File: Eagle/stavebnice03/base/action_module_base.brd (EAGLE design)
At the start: 16 parts

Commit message: I did an order in Eagle files
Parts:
- removed C1, C3, C4, C5: 100nF, resistor:C0603
- removed R1, R2: 4k7, resistor:M0805
- removed U$2, U$3, U$6, U$7: NC7SB3157P6X, !stavebnice03:SC70-6L
- removed U$5: JUMPER5F-90, !stavebnice03:JUMPER5F-90
- added R3: 2K2, resistor:R0603
- added R4: 2k2, resistor:R0603
- moved C2 2.53 mm to (7.50, 9.70), turned to 270 degrees
- moved U$1 0.43 mm to (3.90, 13.3)
- moved U$9 0.25 mm to (5.50, 1.50)
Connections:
- removed net N$1 (its old number): U$1.3, U$6.6, U$7.6
- removed net N$10: R2.1, U$5.2, U$6.3, U$7.1
- removed net N$20: U$2.3, U$7.4
- removed net N$4: U$1.9, U$3.4
- removed net N$6: R1.1, U$5.4, U$6.1, U$7.3
- removed net N$7: U$3.3, U$6.4
- removed net N$8: U$3.1, U$4.2
- removed net N$9: U$1.2, U$2.6, U$3.6
- net GND: no longer C1.2, C3.1, C4.2, C5.1, U$2.2, U$3.2, U$5.1, U$5.5, U$6.2, U$7.2
- net N$2: now also R3.1, U$4.2; no longer U$2.4
- net N$5: now also R4.1, U$1.9; no longer U$2.1
- net VCC: now also R3.2, R4.2, U$1.2, U$1.3; no longer C1.1, C3.2, C4.1, C5.2, R1.2, R2.2, U$2.5, U$3.5, U$5.3, U$6.5, U$7.5
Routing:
- net GND: track 82.6 -> 23.9 mm, vias 2 -> 0
- net N$4: track 27.1 -> 0.00 mm, vias 2 -> 0
- net N$1 (its old number): track 24.3 -> 0.00 mm
- net N$9: track 21.2 -> 0.00 mm, vias 2 -> 0
- net N$20: track 17.6 -> 0.00 mm, vias 2 -> 0
- net N$2: track 9.18 -> 23.1 mm, vias 2 -> 0
- net VCC: track 51.9 -> 39.7 mm, vias 3 -> 0
- net N$13: track 21.8 -> 33.0 mm
- net N$6: track 10.2 -> 0.00 mm, vias 1 -> 0
- net N$10: track 9.64 -> 0.00 mm, vias 1 -> 0
- net N$8: track 5.48 -> 0.00 mm
- net N$5: track 8.92 -> 13.7 mm, vias 1 -> 0
- net N$7: track 3.06 -> 0.00 mm
- net N$14: track 10.9 -> 8.40 mm
- net N$12: track 12.9 -> 11.8 mm
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- added copper zone on layer 16, net N$1
- removed copper zone on layer 16, net N$2
- removed copper zone on layer 1, net N$20
- removed copper zone on layer 16, net N$20
- removed copper zone on layer 1, net N$4
- removed copper zone on layer 16, net N$5
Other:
- board text added: "action module base"
- board text removed: "5 pins - v2"

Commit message: base and battery module size increeased to 22x22
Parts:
- moved U$8 0.50 mm to (13.0, 19.9)
- moved U$9 0.50 mm to (5.50, 1.00)

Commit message: added pin and resistor to stay in bootloader + changed size back to 21x21 mm
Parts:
- added R1: 100k, resistor:R0603
- moved U$9 0.50 mm to (5.10, 1.30)
- moved U$8 0.36 mm to (13.3, 19.7)
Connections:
- new net N$3: R1.2, U$1.2
- net VCC: now also R1.1; no longer U$1.2
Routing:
- net VCC: track 40.2 -> 43.7 mm
- net N$3: track 0.00 -> 3.12 mm, vias 0 -> 1
- net N$5: track 13.7 -> 12.8 mm
- net N$2: track 23.2 -> 22.3 mm
- net N$13: track 33.2 -> 34.0 mm

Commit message: minor element position changes
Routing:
- net N$1: track 10.5 -> 9.94 mm
- removed copper zone on layer 16, net N$1
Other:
- board text added: "action base"
- board text removed: "action module base"
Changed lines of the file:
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@@
 <layer number="21" name="tPlace" color="7" fill="1" visible="no" active="yes"/>
 <layer number="22" name="bPlace" color="7" fill="1" visible="no" active="yes"/>
-<layer number="23" name="tOrigins" color="15" fill="1" visible="yes" active="yes"/>
-<layer number="24" name="bOrigins" color="15" fill="1" visible="yes" active="yes"/>
+<layer number="23" name="tOrigins" color="15" fill="1" visible="no" active="yes"/>
+<layer number="24" name="bOrigins" color="15" fill="1" visible="no" active="yes"/>
 <layer number="25" name="tNames" color="7" fill="1" visible="no" active="yes"/>
 <layer number="26" name="bNames" color="7" fill="1" visible="no" active="yes"/>
@@
 <text x="4.92125" y="-6.0325" size="2.54" layer="16" rot="MR0" align="center">II=I+I</text>
 <text x="4.92125" y="-6.0325" size="2.54" layer="1" align="center">II=I+I</text>
-<text x="10.415" y="29.005" size="1.778" layer="20" align="center">action module base</text>
-<wire x1="-2" y1="-2" x2="23" y2="-2" width="0.05" layer="49"/>
-<wire x1="23" y1="-2" x2="23" y2="23" width="0.05" layer="49"/>
-<wire x1="23" y1="23" x2="-2" y2="23" width="0.05" layer="49"/>
-<wire x1="-2" y1="23" x2="-2" y2="-2" width="0.05" layer="49"/>
+<text x="10.5" y="27" size="1.778" layer="20" align="center">action base</text>
+<wire x1="-10" y1="-10" x2="31" y2="-10" width="0.01" layer="49"/>
+<wire x1="31" y1="-10" x2="31" y2="31" width="0.01" layer="49"/>
+<wire x1="31" y1="31" x2="-10" y2="31" width="0.01" layer="49"/>
+<wire x1="-10" y1="31" x2="-10" y2="-10" width="0.01" layer="49"/>
+<circle x="2.2" y="18.8" radius="0.6" width="0.9" layer="116"/>
+<circle x="18.8" y="2.2" radius="0.6" width="0.9" layer="116"/>
+<circle x="9.34" y="5.42" radius="0.329" width="0.357" layer="116"/>
+<circle x="9.34" y="7.96" radius="0.329" width="0.357" layer="116"/>
+<circle x="9.34" y="10.5" radius="0.329" width="0.357" layer="116"/>
+<circle x="9.34" y="13.04" radius="0.329" width="0.357" layer="116"/>
+<circle x="9.34" y="15.58" radius="0.329" width="0.357" layer="116"/>
+<circle x="19.65" y="19.7" radius="0.329" width="0.357" layer="116"/>
+<circle x="17.11" y="19.7" radius="0.329" width="0.357" layer="116"/>
+<circle x="14.57" y="19.7" radius="0.329" width="0.357" layer="116"/>
+<circle x="12.03" y="19.7" radius="0.329" width="0.357" layer="116"/>
+<circle x="9.49" y="19.7" radius="0.329" width="0.357" layer="116"/>
+<circle x="6.95" y="19.7" radius="0.329" width="0.357" layer="116"/>
+<circle x="1.29" y="1.3" radius="0.329" width="0.357" layer="116"/>
+<circle x="3.83" y="1.3" radius="0.329" width="0.357" layer="116"/>
+<circle x="6.37" y="1.3" radius="0.329" width="0.357" layer="116"/>
+<circle x="8.91" y="1.3" radius="0.329" width="0.357" layer="116"/>
+<circle x="5" y="9" radius="0.225" width="0.15" layer="116"/>
 </plain>
 <attributes>
@@
 <contactref element="U$9" pad="2"/>
 <contactref element="U$1" pad="7"/>
-<polygon width="0.357" layer="16" isolate="0.4064" thermals="no">
-<vertex x="1.5" y="4.9"/>
-<vertex x="6.9" y="2.7"/>
-<vertex x="6.9" y="1.5"/>
-<vertex x="1.4" y="1.5"/>
-<vertex x="1.5" y="4.5"/>
-</polygon>
 <wire x1="1.95" y1="10.475" x2="1.95" y2="4.45" width="0.3556" layer="16"/>
-<wire x1="1.95" y1="4.45" x2="4.4" y2="2" width="0.3556" layer="16"/>
-<wire x1="4.4" y1="2" x2="4.4" y2="1.63" width="0.3556" layer="16"/>
-<wire x1="4.4" y1="1.63" x2="3.83" y2="1.3" width="0.3556" layer="16"/>
+<wire x1="1.95" y1="4.45" x2="3.8" y2="2.6" width="0.3556" layer="16"/>
+<wire x1="3.8" y1="2.6" x2="3.8" y2="1.73" width="0.3556" layer="16"/>
+<wire x1="3.8" y1="1.73" x2="3.83" y2="1.3" width="0.3556" layer="16"/>
 </signal>
 <signal name="N$3">
 <contactref element="U$1" pad="2"/>
 <contactref element="R1" pad="2"/>
-<wire x1="5.2" y1="8.2" x2="5.15" y2="8.15" width="0.3556" layer="16"/>
-<wire x1="5.15" y1="8.15" x2="5.1" y2="7.55" width="0.3556" layer="16"/>
+<wire x1="5.2" y1="8.2" x2="5.25" y2="7.65" width="0.3556" layer="16"/>
+<wire x1="5.25" y1="7.65" x2="5.1" y2="7.55" width="0.3556" layer="16"/>
 <via x="5" y="9" extent="1-16" drill="0.5" diameter="1.27" shape="octagon"/>
 <wire x1="5.2" y1="10.475" x2="5.2" y2="9.4" width="0.3556" layer="16"/>

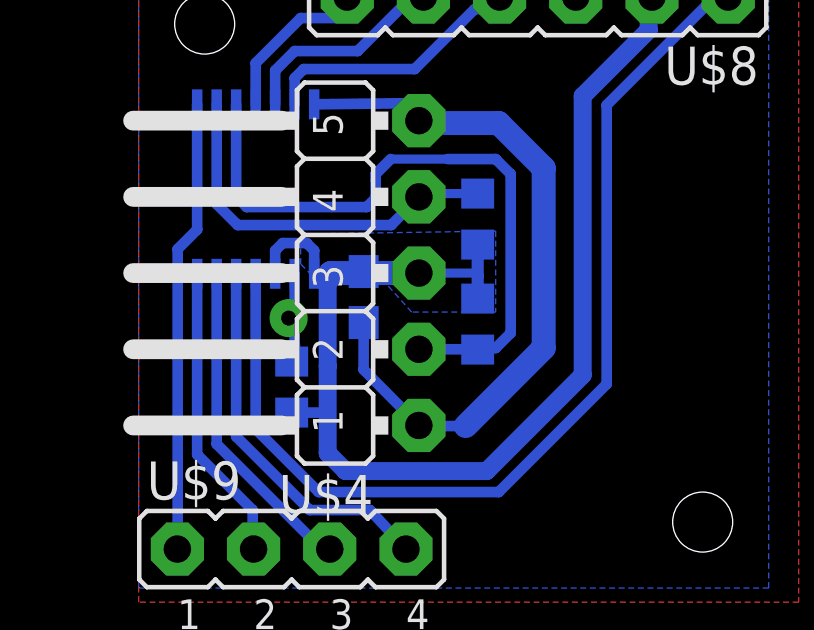
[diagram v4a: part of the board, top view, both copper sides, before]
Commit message: C0603 changed to C0603K with wider space between soldering areas
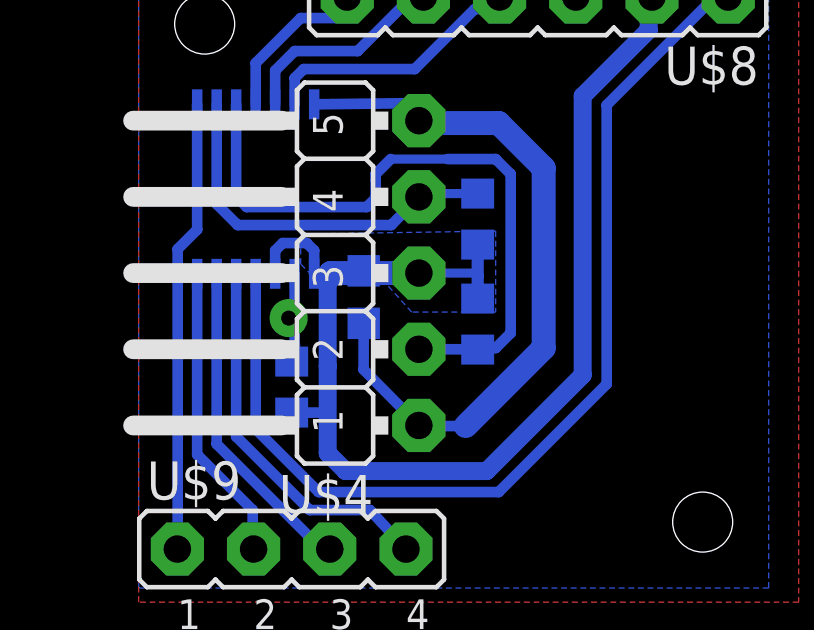
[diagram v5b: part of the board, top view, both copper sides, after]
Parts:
- C2: device resistor:C0603 -> resistor:C0603K
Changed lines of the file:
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@@
 <layer number="22" name="bPlace" color="7" fill="1" visible="no" active="yes"/>
 <layer number="23" name="tOrigins" color="15" fill="1" visible="no" active="yes"/>
-<layer number="24" name="bOrigins" color="15" fill="1" visible="no" active="yes"/>
+<layer number="24" name="bOrigins" color="15" fill="1" visible="yes" active="yes"/>
 <layer number="25" name="tNames" color="7" fill="1" visible="no" active="yes"/>
 <layer number="26" name="bNames" color="7" fill="1" visible="no" active="yes"/>
@@
 <elements>
 <element name="U$1" library="!stavebnice03" package="TSSOP14" value="16F103-TSSOP" x="3.9" y="13.3" rot="MR0"/>
-<element name="C2" library="resistor" package="C0603" value="100nF" x="7.5" y="9.7" rot="MR270"/>
+<element name="C2" library="resistor" package="C0603K" value="100nF" x="7.5" y="9.7" rot="MR270"/>
 <element name="U$4" library="!stavebnice03" package="JUMPER5M-90" value="JUMPER5M-90" x="6.8" y="10.5" rot="R90"/>
 <element name="U$8" library="!stavebnice03" package="JUMPER6M" value="JUMPER6M" x="13.3" y="19.7" rot="R180"/>
@@
 <vertex x="22" y="-0.47"/>
 </polygon>
-<wire x1="7.5" y1="8.85" x2="7.4975" y2="7.2825" width="0.3556" layer="16"/>
+<wire x1="7.5" y1="8.825" x2="7.4975" y2="7.2825" width="0.3556" layer="16"/>
 <wire x1="7.4975" y1="7.2825" x2="9.34" y2="5.42" width="0.3556" layer="16"/>
 <wire x1="9.4" y1="5.4" x2="10.9" y2="5.4" width="0.3556" layer="16"/>
@@
 <contactref element="U$8" pad="2"/>
 <wire x1="9.34" y1="10.5" x2="7.22375" y2="10.5" width="0.8" layer="16"/>
-<wire x1="7.22375" y1="10.5" x2="7.5" y2="10.55" width="0.3556" layer="16"/>
-<wire x1="7.18125" y1="10.51" x2="7.5" y2="10.55" width="0.3556" layer="16"/>
+<wire x1="7.22375" y1="10.5" x2="7.5" y2="10.575" width="0.3556" layer="16"/>
+<wire x1="7.18125" y1="10.51" x2="7.5" y2="10.575" width="0.3556" layer="16"/>
 <wire x1="5.89125" y1="10.49125" x2="5.9" y2="10.5" width="0.3556" layer="16"/>
 <wire x1="5.9" y1="10.5" x2="5.85" y2="10.475" width="0.3556" layer="16"/>
@@
 <wire x1="6.3" y1="10.3" x2="6.4" y2="10.5" width="0.8" layer="16"/>
 <wire x1="6.4" y1="10.5" x2="7.45" y2="10.5" width="0.8" layer="16"/>
-<wire x1="7.45" y1="10.5" x2="7.5" y2="10.55" width="0.8" layer="16"/>
+<wire x1="7.45" y1="10.5" x2="7.5" y2="10.575" width="0.8" layer="16"/>
 <wire x1="5.85" y1="10.475" x2="6.225" y2="10.475" width="0.3556" layer="16"/>
 <wire x1="6.225" y1="10.475" x2="6.3" y2="10.3" width="0.3556" layer="16"/>

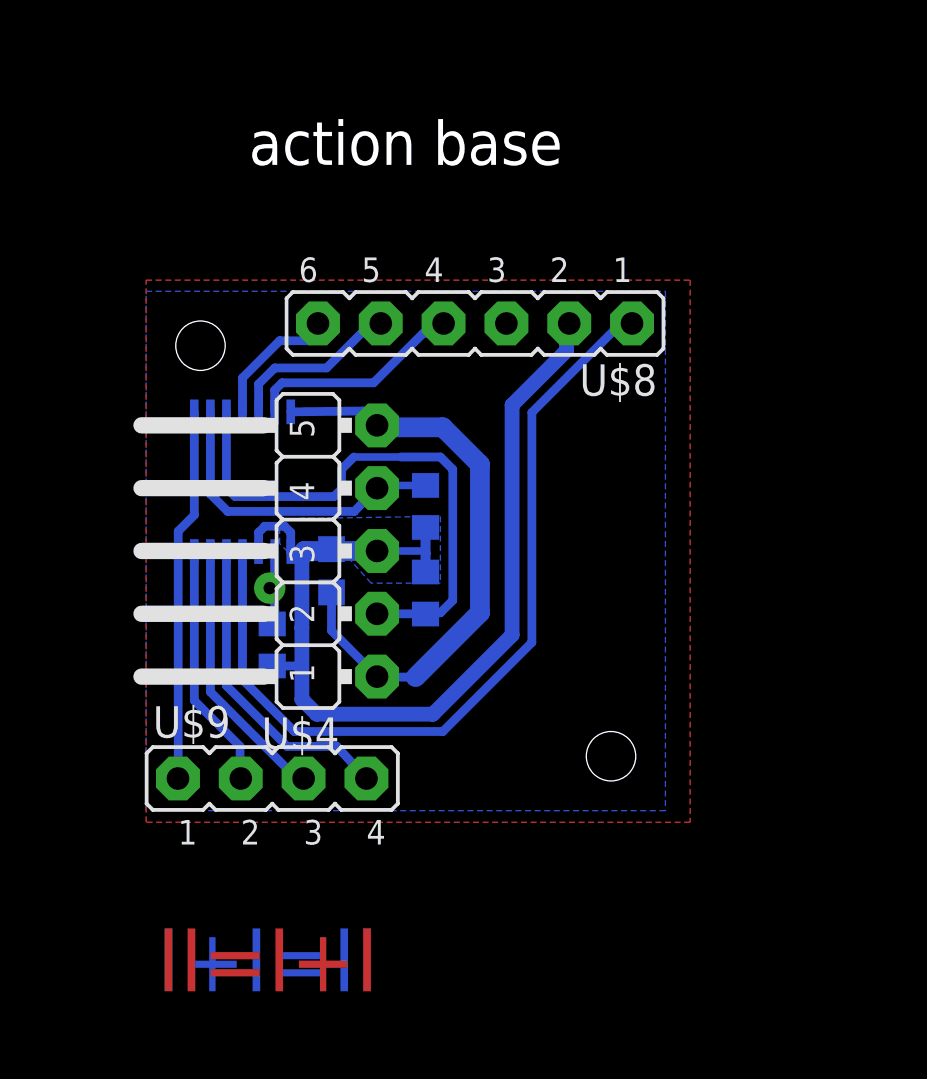
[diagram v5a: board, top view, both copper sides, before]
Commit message: element position changed to be able put the bords to boxes + reset button for source board
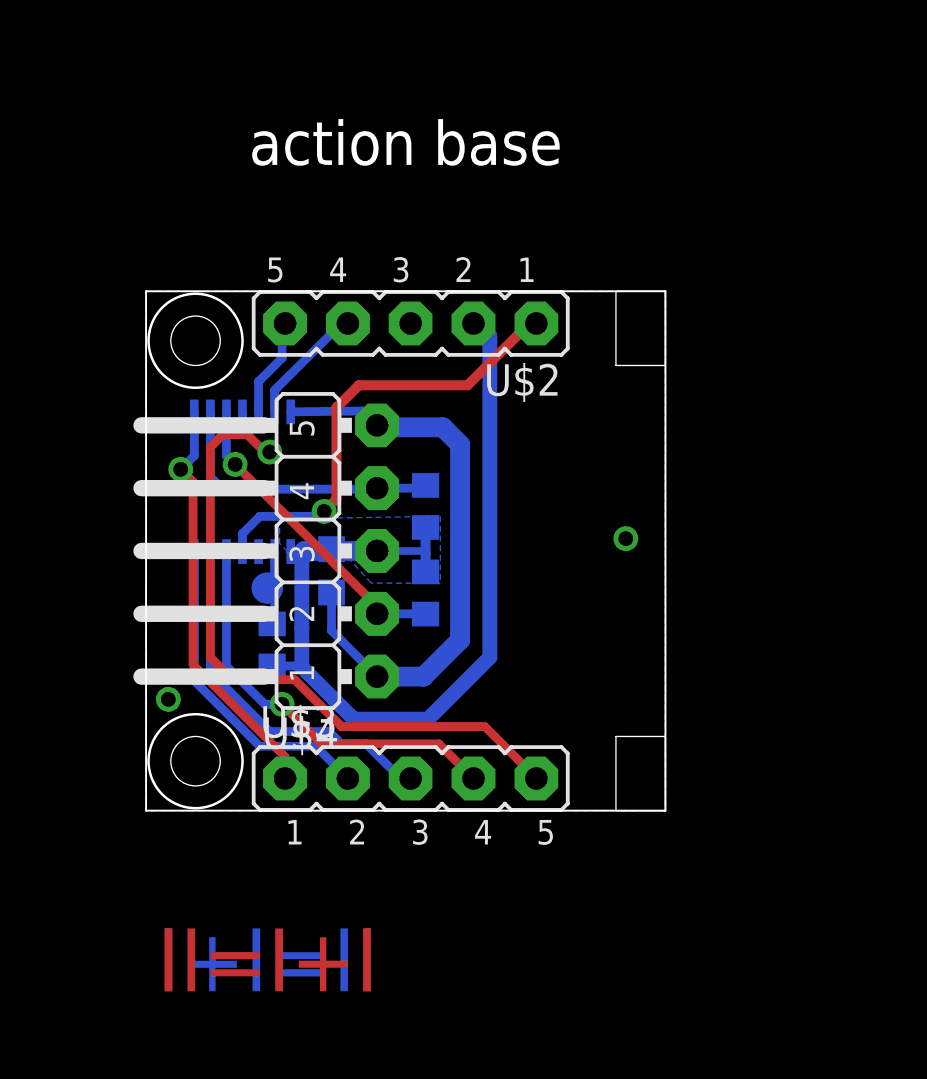
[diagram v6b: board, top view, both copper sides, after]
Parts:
- removed U$8: JUMPER6M, !stavebnice03:JUMPER6M
- removed U$9: JUMPER4M, !stavebnice03:JUMPER4M
- added TP1: TPB1,27, testpad:B1,27
- added U$2, U$3: JUMPER5M, !stavebnice03:JUMPER5M
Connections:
- net GND: now also U$2.3; no longer U$8.3
- net N$1: now also U$3.2; no longer U$9.2
- net N$11: now also U$3.5; no longer U$8.6
- net N$12: now also U$3.4; no longer U$9.4
- net N$13: now also U$2.1; no longer U$8.1
- net N$14: now also U$2.4; no longer U$8.4
- net N$15: now also U$2.5; no longer U$8.5
- net N$17: now also U$3.3; no longer U$9.3
- net N$18: now also U$3.1; no longer U$9.1
- net N$3: now also TP1.TP
- net VCC: now also U$2.2; no longer U$1.3, U$8.2
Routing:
- net N$11: track 5.56 -> 28.8 mm, vias 0 -> 1
- net N$13: track 34.0 -> 18.3 mm, vias 0 -> 1
- net N$2: track 22.3 -> 12.7 mm, vias 0 -> 1
- net VCC: track 43.7 -> 39.1 mm
- net N$14: track 8.82 -> 4.95 mm
- net N$17: track 10.9 -> 14.8 mm
- net N$12: track 12.7 -> 16.5 mm, vias 0 -> 1
- net N$15: track 7.35 -> 4.02 mm
- net N$1: track 9.94 -> 13.1 mm
- net N$18: track 15.1 -> 16.8 mm, vias 0 -> 1
- net N$5: track 12.8 -> 11.6 mm
- net GND: track 23.8 -> 23.4 mm, vias 0 -> 2
- net N$3: track 3.18 -> 3.40 mm, vias 1 -> 0
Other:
- board outline added: 21 x 21 mm

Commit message: layer coloring and place drawing moved to docu layer + changed sizes of names and values
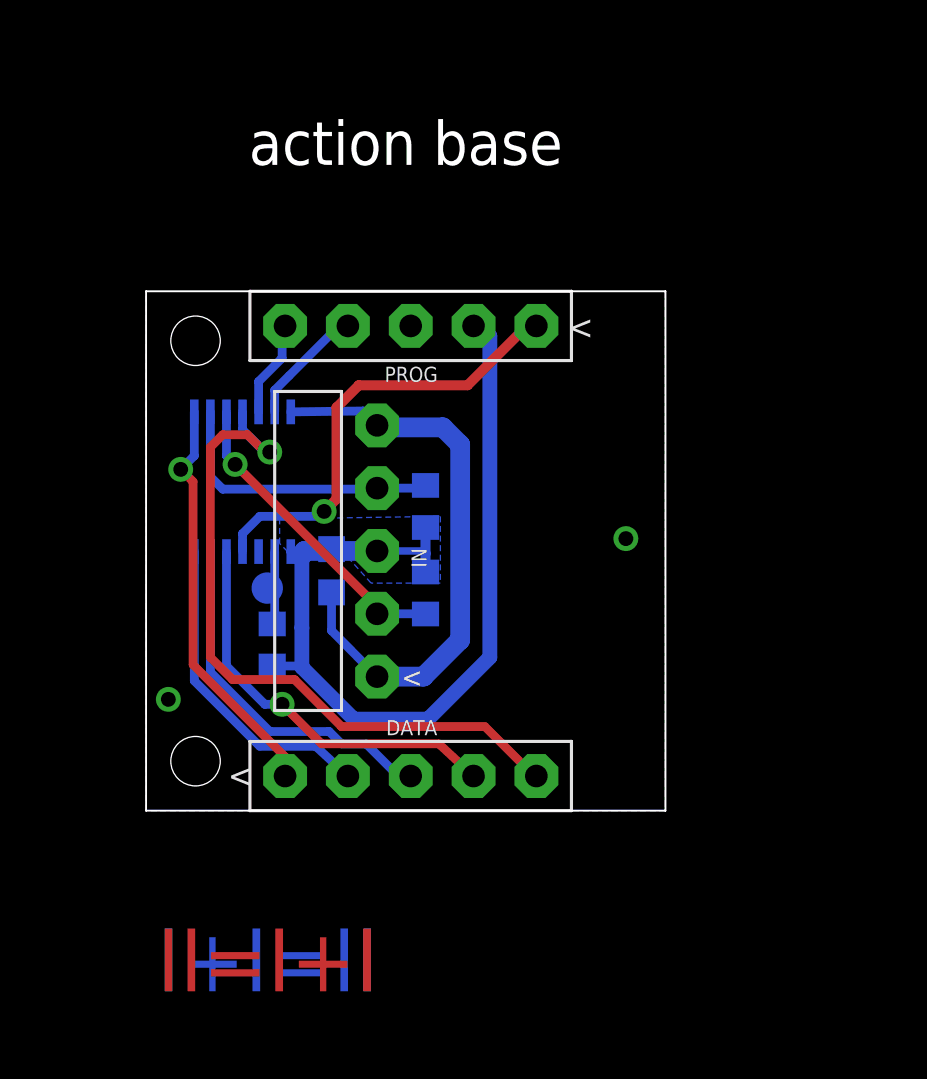
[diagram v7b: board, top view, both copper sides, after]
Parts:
- removed U$2, U$3: JUMPER5M, !stavebnice03:JUMPER5M
- added DATA, PROG: JUMPER5M, !stavebnice03:JUMPER5M
- renumbered U$1 to U1, U$4 to IN
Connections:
- net GND: now also PROG.3; no longer U$2.3
- net N$1: now also DATA.2; no longer U$3.2
- net N$11: now also DATA.5; no longer U$3.5
- net N$12: now also DATA.4; no longer U$3.4
- net N$13: now also PROG.1; no longer U$2.1
- net N$14: now also PROG.4; no longer U$2.4
- net N$15: now also PROG.5; no longer U$2.5
- net N$17: now also DATA.3; no longer U$3.3
- net N$18: now also DATA.1; no longer U$3.1
- net VCC: now also PROG.2; no longer U$2.2
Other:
- outline, holes or cut-outs redrawn

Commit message: eagle adjustment for the Jíťa version
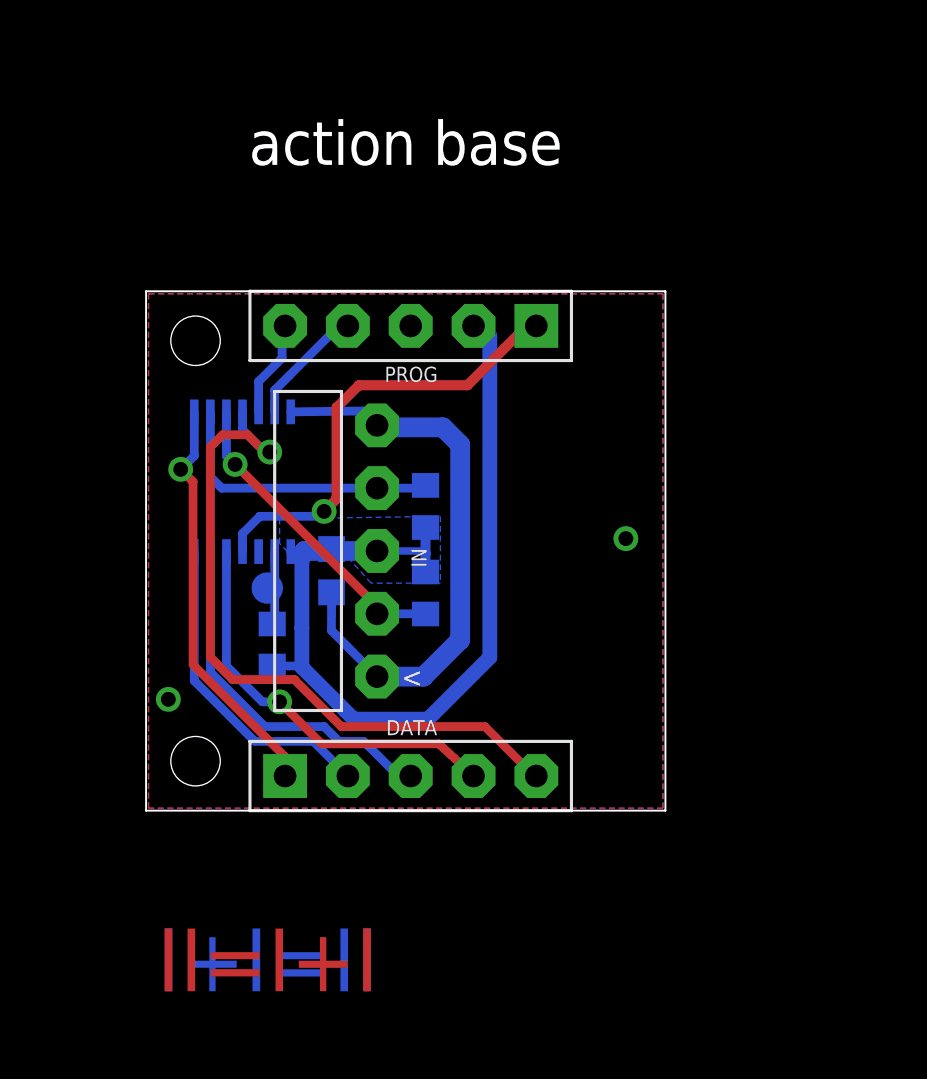
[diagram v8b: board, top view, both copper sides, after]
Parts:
- DATA, PROG: value JUMPER5M -> (none)
- renumbered TP1 to FLASH
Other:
- board text added: "GND"
- board text added: "RA0"
- board text added: "RA1"
- board text added: "RA2"
- board text added: "RA3"
- board text added: "RC2"
- board text added: "RC3"
- board text added: "RC4"
- board text added: "RC5"
- board text added: "VCC"
